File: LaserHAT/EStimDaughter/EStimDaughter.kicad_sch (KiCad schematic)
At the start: 60 parts, among them J1 ELECTRODE E1/E2, J8 J8 power/timing (underside), J9 J9 analog/SPI (underside), U1 ISO7761FDBQR, U2 TLV76050DBZR, U3 TL431 (2.5V), U4 MCP4921-E/MS, U5 OPA2192IDGKR, U6 74HC4053BQ, U7 DG419BDQ, U8 LM393DGKR

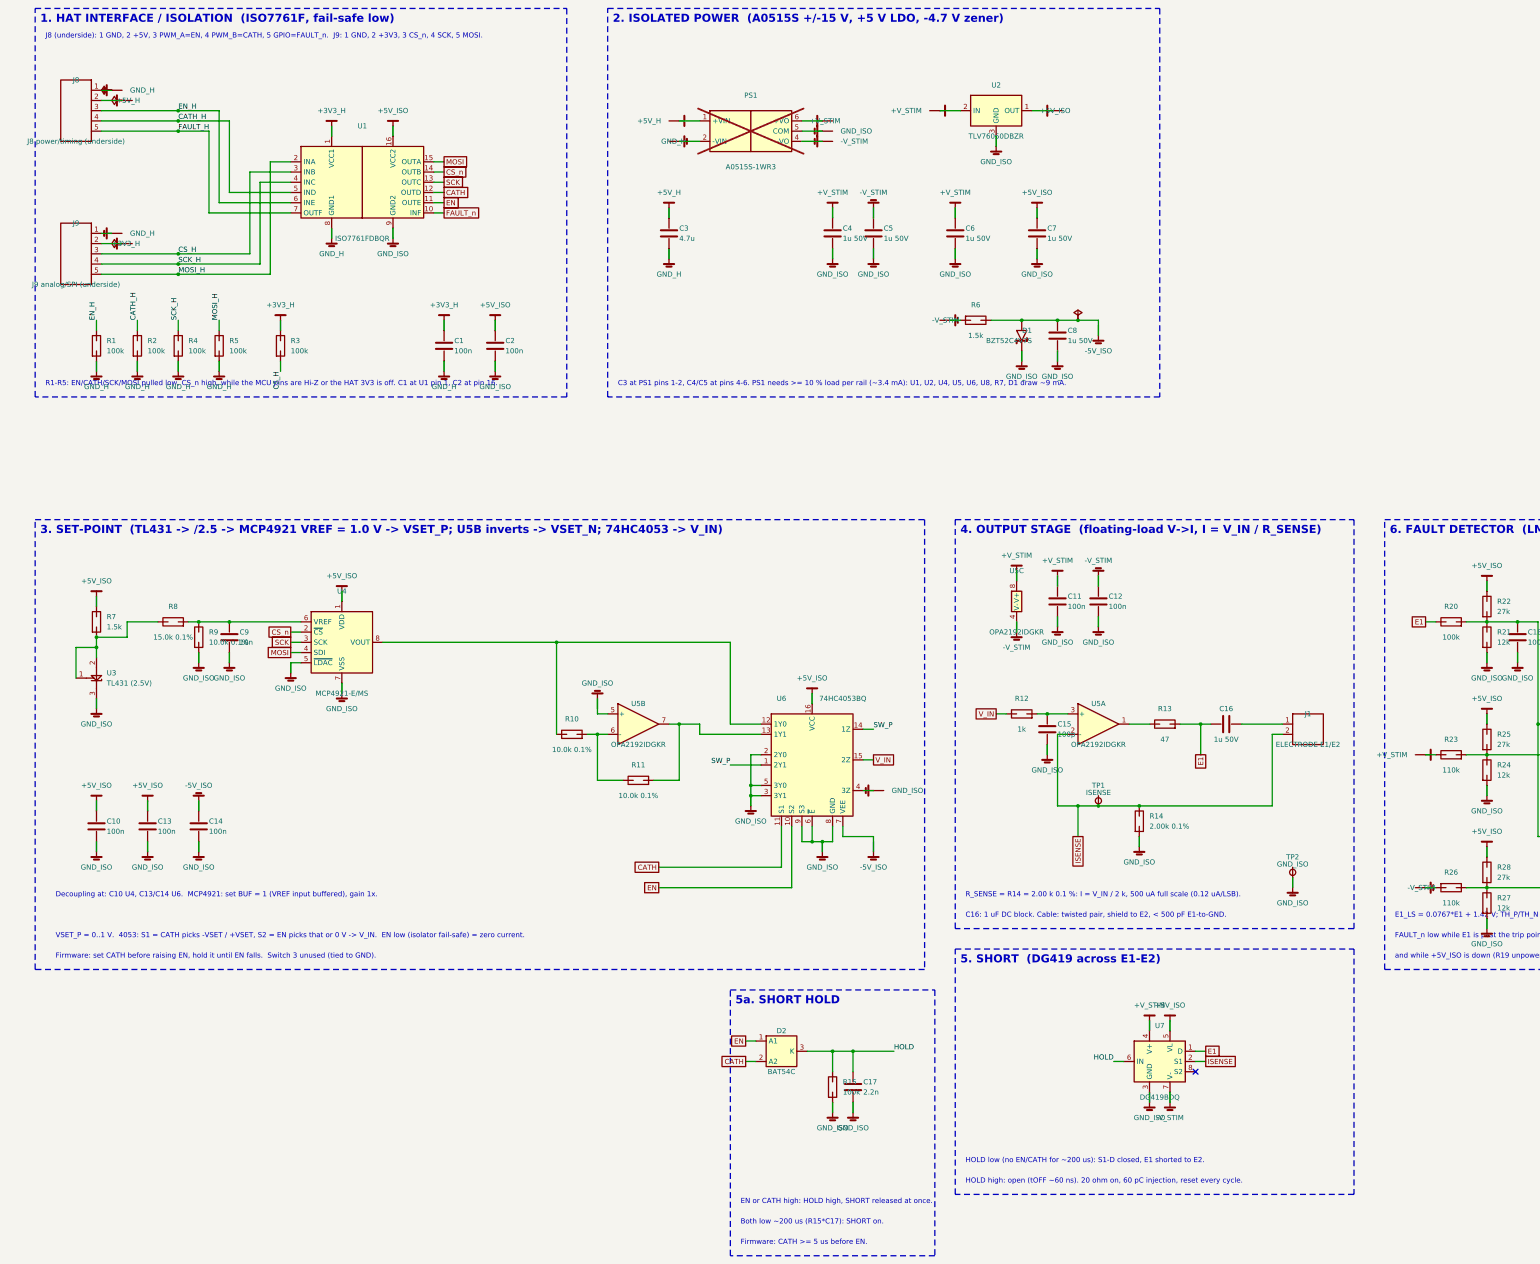
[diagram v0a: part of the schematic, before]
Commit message: EStimDaughter rev M4: I2C DAC (DAC60501 via ISO1640), dedicated RELEASE line for the SHORT switch
- U1 ISO7761F -> ISO7741F (EN, CATH, RELEASE forward; FAULT_n back), new U9 ISO1640
  bidirectional I2C isolator.  J9.3/4/5 = RELEASE / SCL / SDA (HAT NOTICE 13); the HAT's
  copper does not change.
- MCP4921 + TL431 reference chain (U3, R7-R9, C9) -> DAC60501ZDGSR, I2C address 0x48,
  internal 2.5 V reference / 2 = 0-1.25 V; R14 2.00k -> 2.49k 0.1 % (502 uA full scale).
- Hold timer D2/R15/C17 removed: the DG419B is driven by RELEASE (low = shorted; fail-safe
  unchanged).  R3 = RELEASE pull-down, R7/R8 and R9/R15 = 4.7k I2C pull-ups.
- Schematic regenerated (netcheck OK, ERC 0); sims: VREF 1.25 V, R14 2.49k (set-point
  -0.28 %, mismatch -0.005 %).
- PCB: placed only (build_pcb + planes/pours; HAT column to y 106, U9 straddles below U1),
  NOT routed - hand routing follows.  Fab outputs are still the M3 set.
- Docs: README, DESIGN_NOTES (M4 section, firmware contract), spec, NOTICE 13, REV2_NOTES.

Co-Authored-By: Claude Fable 5.1 <noreply@anthropic.com>
Claude-Session: https://claude.ai/code/session_018vgLizGzYPynnY93ajvoVA
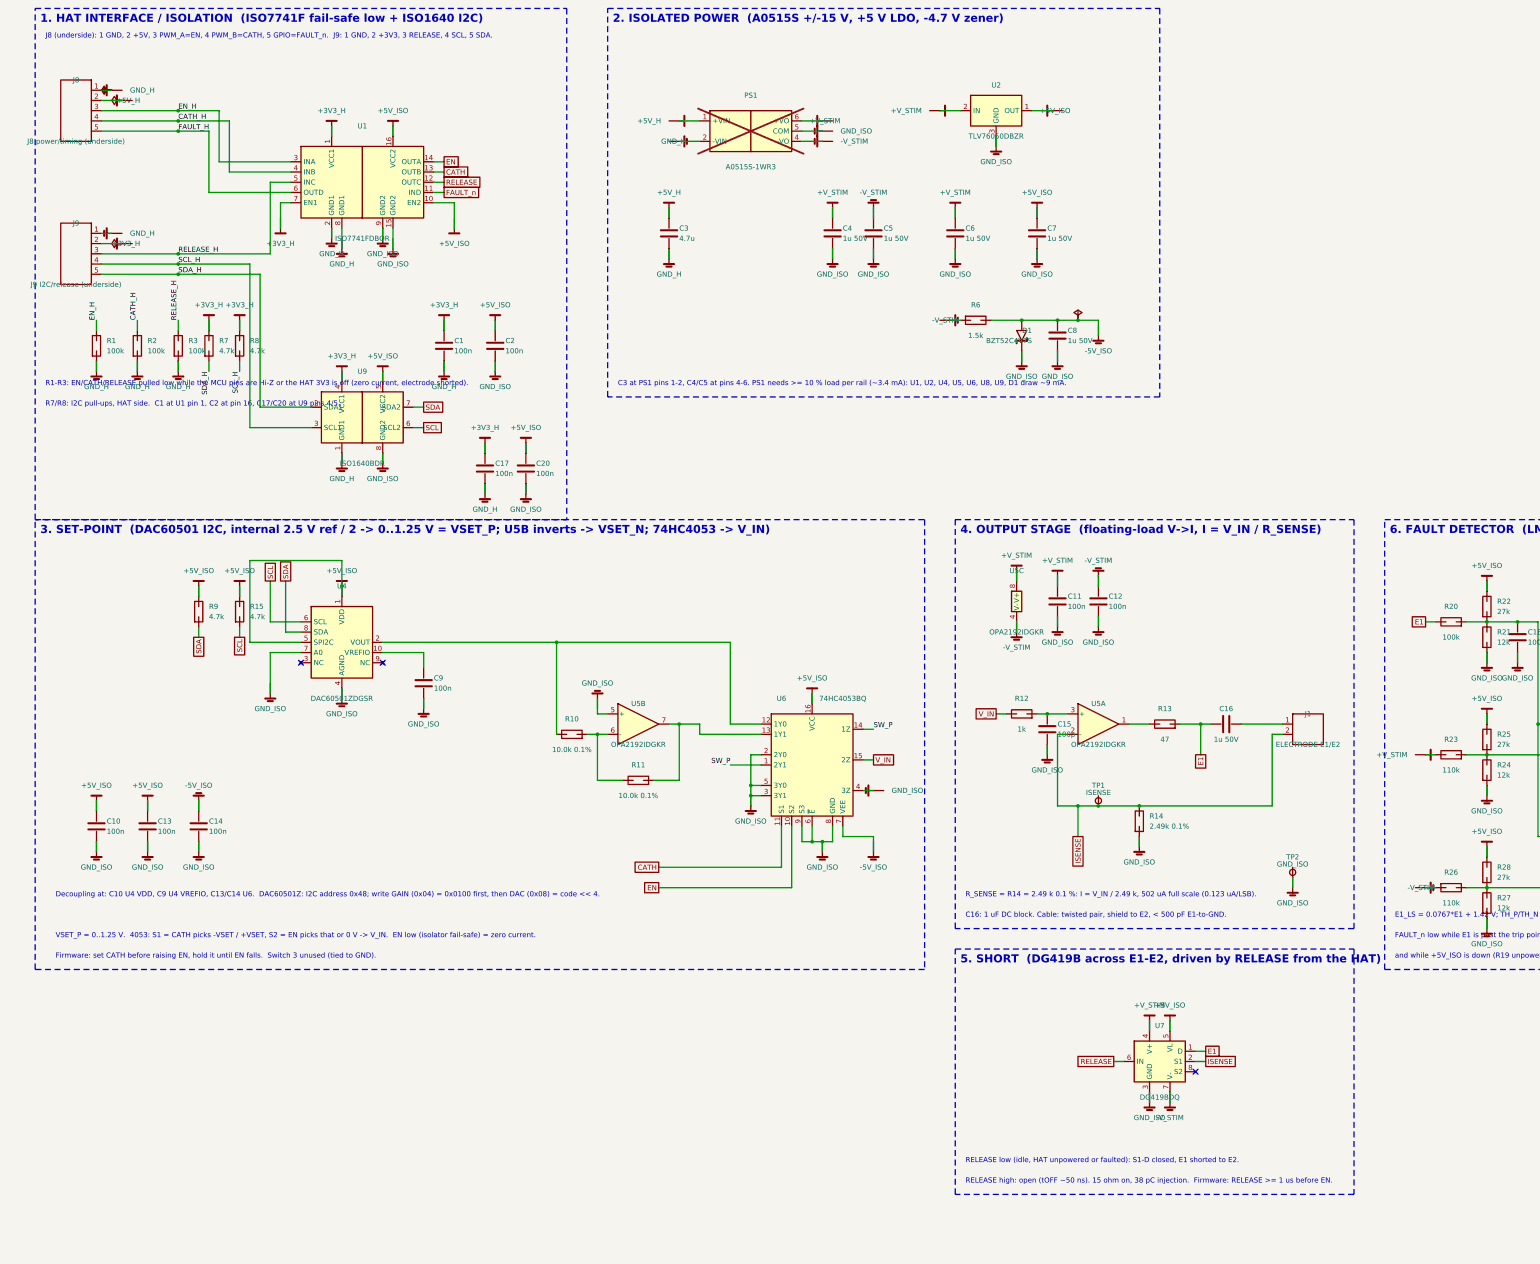
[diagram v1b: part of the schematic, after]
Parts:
- removed D2: BAT54C, Package_TO_SOT_SMD:SOT-23, symbol estim:BAT54C
- removed R4, R5: 100k, Resistor_SMD:R_0402_1005Metric, symbol estim:R
- removed U1: ISO7761FDBQR, Package_SO:SSOP-16_3.9x4.9mm_P0.635mm, symbol estim:ISO7761
- removed U3: TL431 (2.5V), Package_TO_SOT_SMD:SOT-23, symbol estim:TL431_SOT23
- removed U4: MCP4921-E/MS, Package_SO:MSOP-8_3x3mm_P0.65mm, symbol estim:MCP4921
- added C20: 100n, Capacitor_SMD:C_0402_1005Metric, symbol estim:C
- added U1: ISO7741FDBQR, Package_SO:SSOP-16_3.9x4.9mm_P0.635mm, symbol estim:ISO7741
- added U4: DAC60501ZDGSR, Package_SO:VSSOP-10_3x3mm_P0.5mm, symbol estim:DAC60501
- added U9: ISO1640BDR, Package_SO:SOIC-8_3.9x4.9mm_P1.27mm, symbol estim:ISO1640
- C17: value 2.2n -> 100n; LCSC C106861 -> C1525
- C9: value 10n -> 100n; LCSC C15195 -> C1525
- J9: value J9 analog/SPI (underside) -> J9 I2C/release (underside)
- R14: value 2.00k 0.1% -> 2.49k 0.1%; LCSC C328425 -> C861299
- R15: value 100k -> 4.7k; LCSC C25741 -> C25900
- R7: value 1.5k -> 4.7k; footprint Resistor_SMD:R_0603_1608Metric -> Resistor_SMD:R_0402_1005Metric; LCSC C22843 -> C25900
- R8: value 15.0k 0.1% -> 4.7k; footprint Resistor_SMD:R_0603_1608Metric -> Resistor_SMD:R_0402_1005Metric; LCSC C326733 -> C25900
- R9: value 10.0k 0.1% -> 4.7k; footprint Resistor_SMD:R_0603_1608Metric -> Resistor_SMD:R_0402_1005Metric; LCSC C95204 -> C25900
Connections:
- net MOSI_H is gone; now on net SDA_H: J9.5 (Pin_5)
- net +3V3_H: now also C17.1, R7.1, R8.1, U1.1 (VCC1), U1.7 (EN1), U9.4 (VCC1); no longer R3.1
- net +5V_ISO: now also R15.1, R9.1, C20.1, U1.10 (EN2), U1.16 (VCC2), U4.1 (VDD), U4.5 (SPI2C), U9.5 (VCC2); no longer R7.1
- net CATH: now also U1.13 (OUTB)
- net CATH_H: now also U1.4 (INB)
- net EN: now also U1.14 (OUTA)
- net EN_H: now also U1.3 (INA)
- net FAULT_H: now also U1.6 (OUTD)
- net FAULT_n: now also U1.11 (IND)
- net GND_H: now also C17.2, R3.2, U1.2 (GND1), U1.8 (GND1), U9.1 (GND1)
- net GND_ISO: now also C20.2, U1.15 (GND2), U1.9 (GND2), U4.4 (AGND), U4.7 (A0), U9.8 (GND2); no longer C17.2, R15.2, R9.2
- net at R10.1, U6.12 (1Y0): now also U4.2 (VOUT)
- net SDA_H: now reaches R7.2
- net SDA_H: now also U9.2 (SDA1); no longer R8.1
- net CS_H renamed RELEASE_H
- net RELEASE_H: now also R3.1, U1.5 (INC); no longer R3.2
- removed net HOLD: C17.1, R15.1, U7.6 (IN)
- net SCK_H renamed SCL_H
- net SCL_H: now also R8.2, U9.3 (SCL1)
- new net: C9.1, U4.10 (VREFIO)
- new net RELEASE: U1.12 (OUTC), U7.6 (IN)
- new net SCL: R15.2, U4.6 (SCL), U9.6 (SCL2)
- new net SDA: R9.2, U4.8 (SDA), U9.7 (SDA2)
- no-connect marks 1 -> 3
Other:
- note added: "1. HAT INTERFACE / ISOLATION (ISO7741F fail-safe low + ISO1640 I2C)"
- note added: "3. SET-POINT (DAC60501 I2C, internal 2.5 V ref / 2 -> 0..1.25 V = VSET_P; U5B inverts -> VSET_N; 74HC4053 -> V_IN)"
- note added: "5. SHORT (DG419B across E1-E2, driven by RELEASE from the HAT)"
- note added: "C3 at PS1 pins 1-2, C4/C5 at pins 4-6. PS1 needs >= 10 % load per rail (~3.4 mA): U1, U2, U4, U5, U6, U8, U9, D1 draw ~9 mA."
- note added: "Decoupling at: C10 U4 VDD, C9 U4 VREFIO, C13/C14 U6. DAC60501Z: I2C address 0x48; write GAIN (0x04) = 0x0100 first, then DAC (0x08) = code << 4."
- note added: "J8 (underside): 1 GND, 2 +5V, 3 PWM_A=EN, 4 PWM_B=CATH, 5 GPIO=FAULT_n. J9: 1 GND, 2 +3V3, 3 RELEASE, 4 SCL, 5 SDA."
- note added: "R1-R3: EN/CATH/RELEASE pulled low while the MCU pins are Hi-Z or the HAT 3V3 is off (zero current, electrode shorted)."
- note added: "R7/R8: I2C pull-ups, HAT side. C1 at U1 pin 1, C2 at pin 16, C17/C20 at U9 pins 4/5."
- note added: "RELEASE high: open (tOFF ~50 ns). 15 ohm on, 38 pC injection. Firmware: RELEASE >= 1 us before EN."
- note added: "RELEASE low (idle, HAT unpowered or faulted): S1-D closed, E1 shorted to E2."
- note added: "R_SENSE = R14 = 2.49 k 0.1 %: I = V_IN / 2.49 k, 502 uA full scale (0.123 uA/LSB)."
- note added: "VSET_P = 0..1.25 V. 4053: S1 = CATH picks -VSET / +VSET, S2 = EN picks that or 0 V -> V_IN. EN low (isolator fail-safe) = zero current."
- note removed: "1. HAT INTERFACE / ISOLATION (ISO7761F, fail-safe low)"
- note removed: "3. SET-POINT (TL431 -> /2.5 -> MCP4921 VREF = 1.0 V -> VSET_P; U5B inverts -> VSET_N; 74HC4053 -> V_IN)"
- note removed: "5. SHORT (DG419 across E1-E2)"
- note removed: "5a. SHORT HOLD"
- note removed: "Both low ~200 us (R15*C17): SHORT on."
- note removed: "C3 at PS1 pins 1-2, C4/C5 at pins 4-6. PS1 needs >= 10 % load per rail (~3.4 mA): U1, U2, U4, U5, U6, U8, R7, D1 draw ~9 mA."
- note removed: "Decoupling at: C10 U4, C13/C14 U6. MCP4921: set BUF = 1 (VREF input buffered), gain 1x."
- note removed: "EN or CATH high: HOLD high, SHORT released at once."
- note removed: "Firmware: CATH >= 5 us before EN."
- note removed: "HOLD high: open (tOFF ~60 ns). 20 ohm on, 60 pC injection, reset every cycle."
- note removed: "HOLD low (no EN/CATH for ~200 us): S1-D closed, E1 shorted to E2."
- note removed: "J8 (underside): 1 GND, 2 +5V, 3 PWM_A=EN, 4 PWM_B=CATH, 5 GPIO=FAULT_n. J9: 1 GND, 2 +3V3, 3 CS_n, 4 SCK, 5 MOSI."
- note removed: "R1-R5: EN/CATH/SCK/MOSI pulled low, CS_n high, while the MCU pins are Hi-Z or the HAT 3V3 is off. C1 at U1 pin 1, C2 at pin 16."
- note removed: "R_SENSE = R14 = 2.00 k 0.1 %: I = V_IN / 2 k, 500 uA full scale (0.12 uA/LSB)."
- note removed: "VSET_P = 0..1 V. 4053: S1 = CATH picks -VSET / +VSET, S2 = EN picks that or 0 V -> V_IN. EN low (isolator fail-safe) = zero current."

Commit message: EStimDaughter: L-shaped isolation barrier on all layers, isolator channels follow the placement, J9.4/J9.5 = SDA/SCL
- Barrier is now a plain L (y 83.58 to x 120, x 120 down to y 95.5, then east); GND_H / GND_ISO
  zones on F, In1, In2 and B share the same two outlines; rule areas ISOLATION_BARRIER_0/1/2.
- U1 ISO7741F channels A/B/C = RELEASE/CATH/EN so J8.3/J8.4 and J9.3 drop straight in. FAULT_n
  stays on J8.5: PA6 is the MCU's only TIMA0 fault pin (one via needed).
- J9.4 = SDA, J9.5 = SCL (spec section 7); U9 ISO1640 channels swapped with it so the DAC
  connects without crossings. HAT firmware change only (PA17 = SDA, PA22 = SCL); open question
  for the HAT session in LAYOUT_HANDOFF.md.
- Schematic regenerated (netcheck OK); DRC has no new violations.

Co-Authored-By: Claude Fable 5.1 <noreply@anthropic.com>
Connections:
- net EN: now also U1.12 (OUTC); no longer U1.14 (OUTA)
- net EN_H: now also U1.5 (INC); no longer U1.3 (INA)
- net RELEASE: now also U1.14 (OUTA); no longer U1.12 (OUTC)
- net RELEASE_H: now also U1.3 (INA); no longer U1.5 (INC)
- net SCL: now also U9.7 (SDA2); no longer U9.6 (SCL2)
- net SCL_H: now also J9.5 (Pin_5), U9.2 (SDA1); no longer J9.4 (Pin_4), U9.3 (SCL1)
- net SDA: now also U9.6 (SCL2); no longer U9.7 (SDA2)
- net SDA_H: now also J9.4 (Pin_4), U9.3 (SCL1); no longer J9.5 (Pin_5), U9.2 (SDA1)
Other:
- note added: "J8 (underside): 1 GND, 2 +5V, 3 PWM_A=EN, 4 PWM_B=CATH, 5 GPIO=FAULT_n. J9: 1 GND, 2 +3V3, 3 RELEASE, 4 SDA, 5 SCL."
- note removed: "J8 (underside): 1 GND, 2 +5V, 3 PWM_A=EN, 4 PWM_B=CATH, 5 GPIO=FAULT_n. J9: 1 GND, 2 +3V3, 3 RELEASE, 4 SCL, 5 SDA."
